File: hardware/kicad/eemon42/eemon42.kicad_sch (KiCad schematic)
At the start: 81 parts, among them J1 Barrel_Jack, J17 Conn_02x03_Odd_Even, J37 USB_B_Micro, J4 Barrel_Jack, SW2 SW_MEC_5E, SW3 SW_MEC_5E, SW4 SW_MEC_5E, U1 ESP32-C3-WROOM-02-N4, U11 PL133-97QC, U12 PEC12R-4117F-S0012, U3 16.384MHz, U8 TPS5403

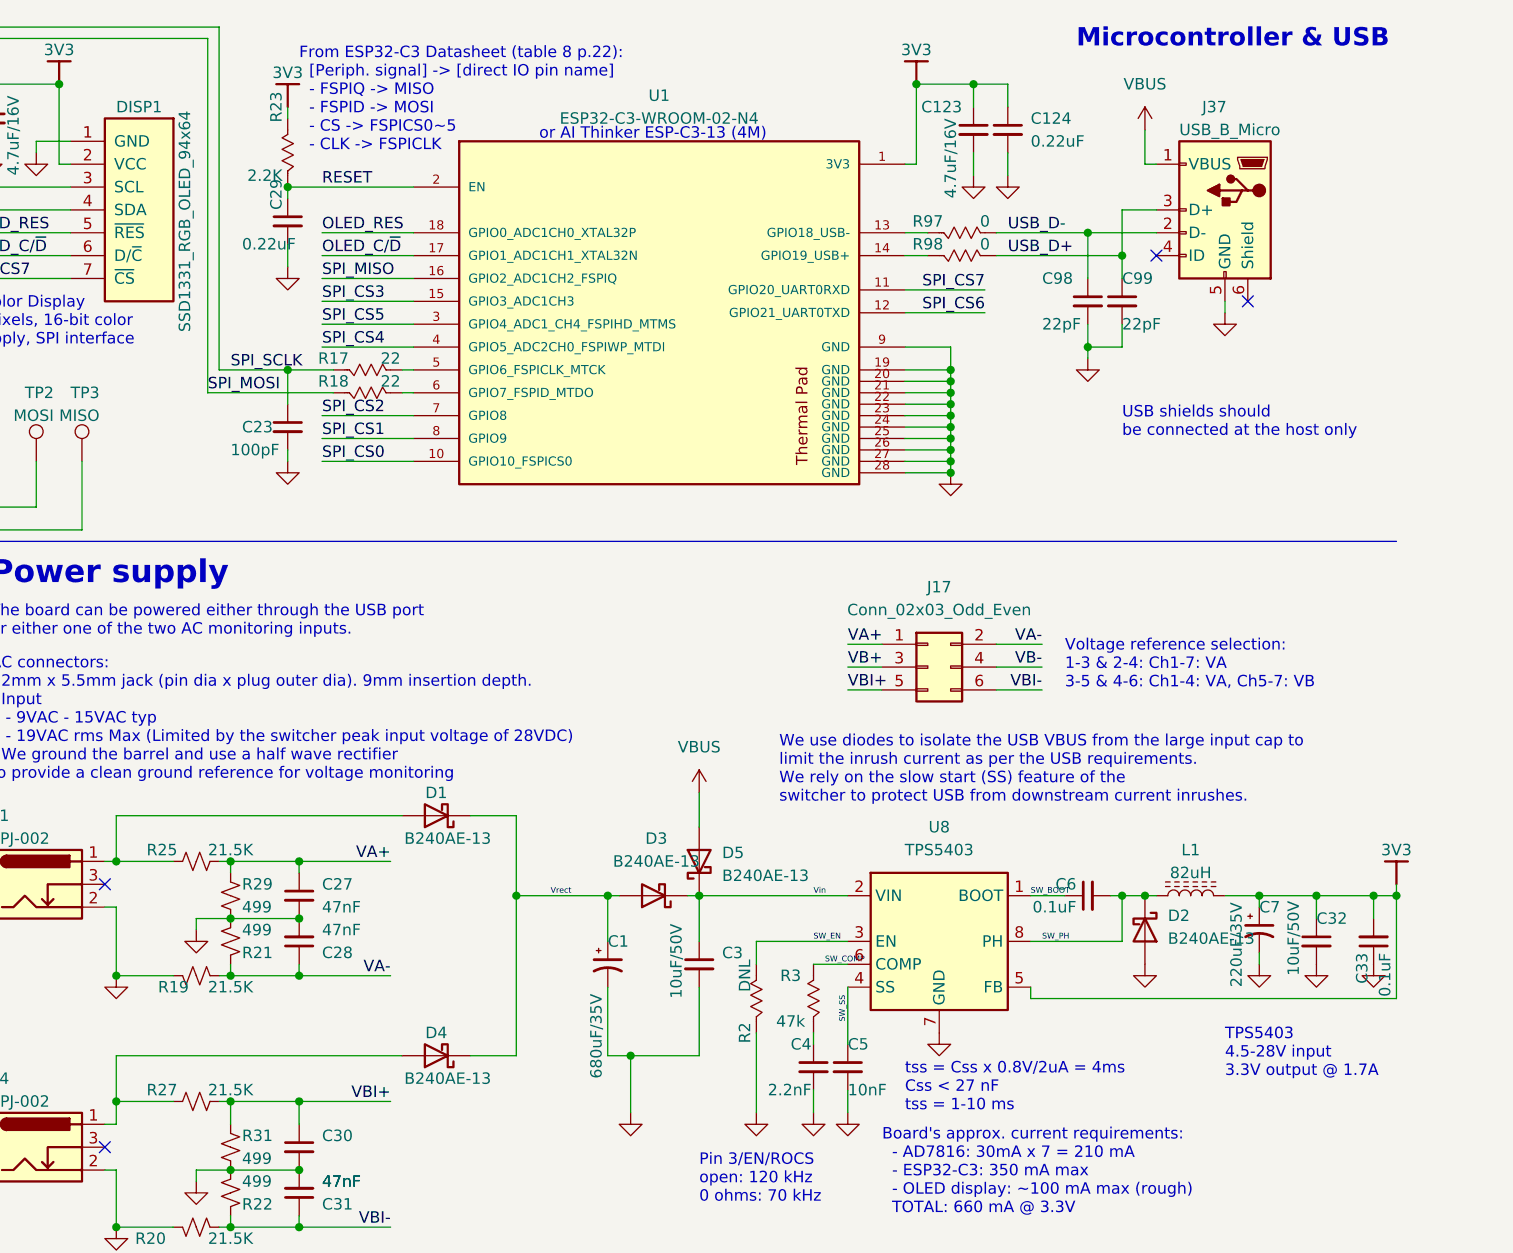
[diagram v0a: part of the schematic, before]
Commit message: Schematics update: Added pullups on GPIO2 & 8. Shuffles CS lines so OLED CS7 is on FSPICS0 (for native toggling), CS2 is on GPO9 so encoder button can control boot mode. CS0 and CS1 are displaced.
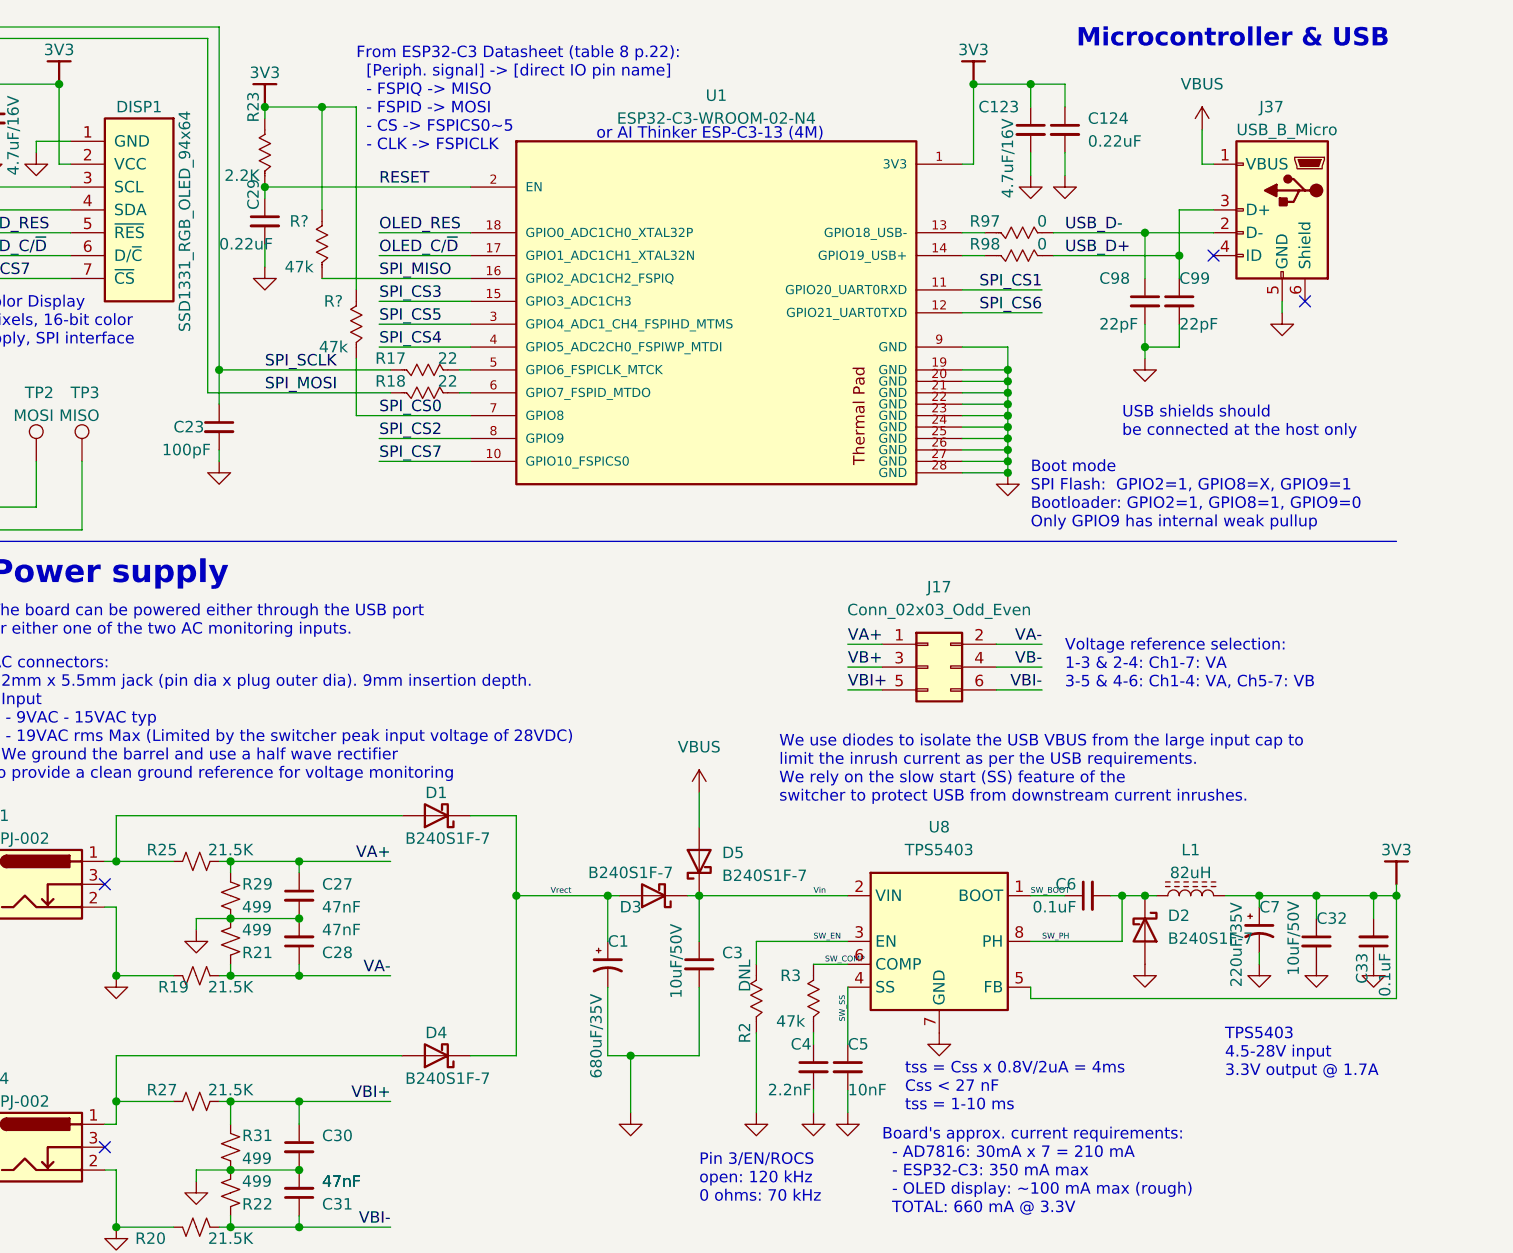
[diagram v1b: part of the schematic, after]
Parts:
- added R? (x2): 47k, Resistor_SMD:R_0603_1608Metric, symbol emon36:R_US
- D1, D2, D3, D4, D5: value B240AE-13 -> B240S1F-7; MPN B240AE-13 -> B240S1F-7
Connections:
- net 3V3: now also R?.1, R?.1
- net SPI_CS0: now also U1.7 (GPIO8), R?.2; no longer U1.10 (GPIO10_FSPICS0)
- net SPI_CS1: now also U1.11 (GPIO20_UART0RXD); no longer U1.8 (GPIO9)
- net SPI_CS2: now also U1.8 (GPIO9); no longer U1.7 (GPIO8)
- net SPI_CS7: now also U1.10 (GPIO10_FSPICS0); no longer U1.11 (GPIO20_UART0RXD)
- net SPI_MISO: now also R?.2
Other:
- note added: "Boot mode SPI Flash: GPIO2=1, GPIO8=X, GPIO9=1 Bootloader: GPIO2=1, GPIO8=1, GPIO9=0 Only GPIO9 has internal weak pullup"
- title: EEMON42 - 36-channel single-board energy monitor -> EEMON42 - 42-channel single-board energy monitor
- moved on the sheet: C123, C124, C23, C29, C98, C99, J37, R17, R18, R23, R97, R98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
